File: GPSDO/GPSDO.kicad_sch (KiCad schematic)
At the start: 119 parts, among them IC4 74HC14, IC5 74HC14, IC7 74HC14, IC8 74HC14, J11 JP1, J2 SolderJumper_3_Open, J3 SolderJumper_2_Open, K1 Conn_01x04, K10 Conn_Coaxial, K3 Conn_01x02, K4 Conn_Coaxial, K5 Jumper_3_Open, K6 Conn_Coaxial, K7 Conn_01x02, K8 Conn_Coaxial, K9 Conn_Coaxial, U1 LM7805_TO220, U2 DAC8571IDGK, U3 Pico, U4 AD8620, U5 74LVC2G86, U6 LM4040DBZ-4.1, U8 U1, U9 CAT24C128

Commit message: Layout almost done (GND plane & edge cuts missing), replaced counters with PIC 12F675 MCU for more flexible down conversion and less ICs on the PCB
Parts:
- removed C36, C37: 100n, Capacitor_SMD:C_1210_3225Metric_Pad1.33x2.70mm_HandSolder, symbol Device:C
- removed IC3, IC6: ~, Package_SO:SOIC-16_3.9x9.9mm_P1.27mm, symbol GPSDO-Components:CD74HC390_1
- removed IC4, IC5, IC8: 74HC14, Package_SO:SOIC-14_3.9x8.7mm_P1.27mm, symbol 74xx:74HC14
- removed J11: JP1, Connector_PinHeader_2.54mm:PinHeader_2x03_P2.54mm_Vertical, symbol Connector_Generic:Conn_02x03_Counter_Clockwise
- removed J2: SolderJumper_3_Open, Jumper:SolderJumper-3_P1.3mm_Open_RoundedPad1.0x1.5mm_NumberLabels, symbol Jumper:SolderJumper_3_Open
- removed J3: SolderJumper_2_Open, Jumper:SolderJumper-2_P1.3mm_Open_RoundedPad1.0x1.5mm, symbol Jumper:SolderJumper_2_Open
- removed L11: 10µ, Inductor_SMD:L_0805_2012Metric_Pad1.15x1.40mm_HandSolder, symbol Device:L
- added JP2: Conn_02x03_Odd_Even, Connector_PinHeader_2.54mm:PinHeader_2x03_P2.54mm_Vertical, symbol Connector_Generic:Conn_02x03_Odd_Even
- added U10, U7: 74HC14, Package_SO:SOIC-14_3.9x8.7mm_P1.27mm, symbol 74xx:74HC14
- added U11: PIC12F675-xP, Package_DIP:DIP-8_W7.62mm, symbol MCU_Microchip_PIC12:PIC12F675-xP
- C11, C3: footprint Capacitor_THT:C_Rect_L7.2mm_W3.5mm_P5.00mm_FKS2_FKP2_MKS2_MKP2 -> Capacitor_THT:C_Rect_L7.2mm_W5.5mm_P5.00mm_FKS2_FKP2_MKS2_MKP2
- C17, C2, C21, C7: footprint Capacitor_THT:CP_Radial_D6.3mm_P2.50mm -> Capacitor_SMD:CP_Elec_4x5.3
- C18, C5: footprint Capacitor_THT:CP_Radial_D10.0mm_P5.00mm -> Capacitor_SMD:CP_Elec_6.3x9.9
- D1: footprint Diode_SMD:D_SMA-SMB_Universal_Handsoldering -> Diode_SMD:D_SOD-123F
- D2: footprint Diode_THT:D_DO-15_P10.16mm_Horizontal -> Diode_SMD:D_SMB
- K7: footprint Connector_BarrelJack:BarrelJack_CUI_PJ-102AH_Horizontal -> Connector_AMASS:AMASS_XT30PW-M_1x02_P2.50mm_Horizontal
- R1, R10, R11, R12, R13, R14, R15, R16, R17, R18, R19, R2, R20, R21, R22, R23, R24, R25, R26, R27, R28, R29, R3, R30, R31, R32, R33, R34, R35, R36, R37, R38, R39, R4, R40, R41, R42, R43, R5, R6, R7, R8, R9: footprint Resistor_SMD:R_1210_3225Metric_Pad1.30x2.65mm_HandSolder -> Resistor_SMD:R_0805_2012Metric_Pad1.20x1.40mm_HandSolder
- RV1: footprint Potentiometer_THT:Potentiometer_Bourns_3266Y_Vertical -> Potentiometer_SMD:Potentiometer_Bourns_3314S_Horizontal
- RV2: footprint Potentiometer_THT:Potentiometer_Bourns_3266Y_Vertical -> Potentiometer_SMD:Potentiometer_Bourns_3314J_Vertical
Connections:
- net GND: now also JP2.5 (Pin_5), JP2.6 (Pin_6), U10.7 (GND), U11.8 (VSS), U7.7 (GND)
- net VCC: no longer R3.1
- net at L7.2: now also C26.2, U11.1 (VDD)
- net at R29.1: now also U11.7 (GP0)
- net at U5.7: now also U7.1, U7.11, U7.13, U7.3
- net at R34.2: now also U7.10
- net at U8.5 (CLK): now also U10.11, U10.3, U10.5, U10.9
- net at R18.2: now also U10.4
- net at U5.3: now also U10.1, U10.13, U7.5, U7.9
- net at R21.2: now also U7.6
- net at R30.2: now also U7.8
- net at R18.1, R40.1, R42.1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: now also K10.1 (In)
- net at R43.2: now also U10.10
- net at C35.1, L2.1, R38.2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: now also R3.1
- net at U8.4 (S1): now also JP2.3 (Pin_3)
- net at U8.6 (S0): now also JP2.4 (Pin_4)
- net at C25.2, L6.2: now also U10.14 (VCC)
- net at IC7.11, IC7.13, IC7.2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: now also U11.2 (GP5)
- net at R42.2: now also U10.8
- net at C24.2, L4.2: now also U7.14 (VCC)
- net at R40.2: now also U10.6
- net at R31.2: now also U10.2
- net at R32.2: now also U10.12
- net at R39.2: now also JP2.2 (Pin_2)
- net at R33.2: now also U7.4
- net at R38.1: now also JP2.1 (Pin_1)
- net at R41.2: now also U7.12
- net at R19.2: now also U7.2
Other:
- note added: "10MHz_in"
- note added: "1kHz/10kHz/100kHz from GPS module"
- note added: "CLK_out"
- note added: "D2 Entstördiode https://www.mouser.de/ProductDetail/Micro-Commercial-Components-MCC/SMBJP6KE6.8CA-TP?qs=O1HRStiETCjFEvwWmakxhQ%3D%3D"
- note removed: "100kHz"
- note removed: "10kHz"
- note removed: "1MHz"
- note removed: "1kHz"
- note removed: "Bypass IC3"
- note removed: "D2 Entstördiode https://www.mouser.de/ProductDetail/Nexperia/PESD5V5H1BSFYL?qs=T3oQrply3y9CfA%2FMHqAcog%3D%3D"
- note removed: "close: f_comp=100kHz"
- moved on the sheet: C24, C25, K10, L4, L6

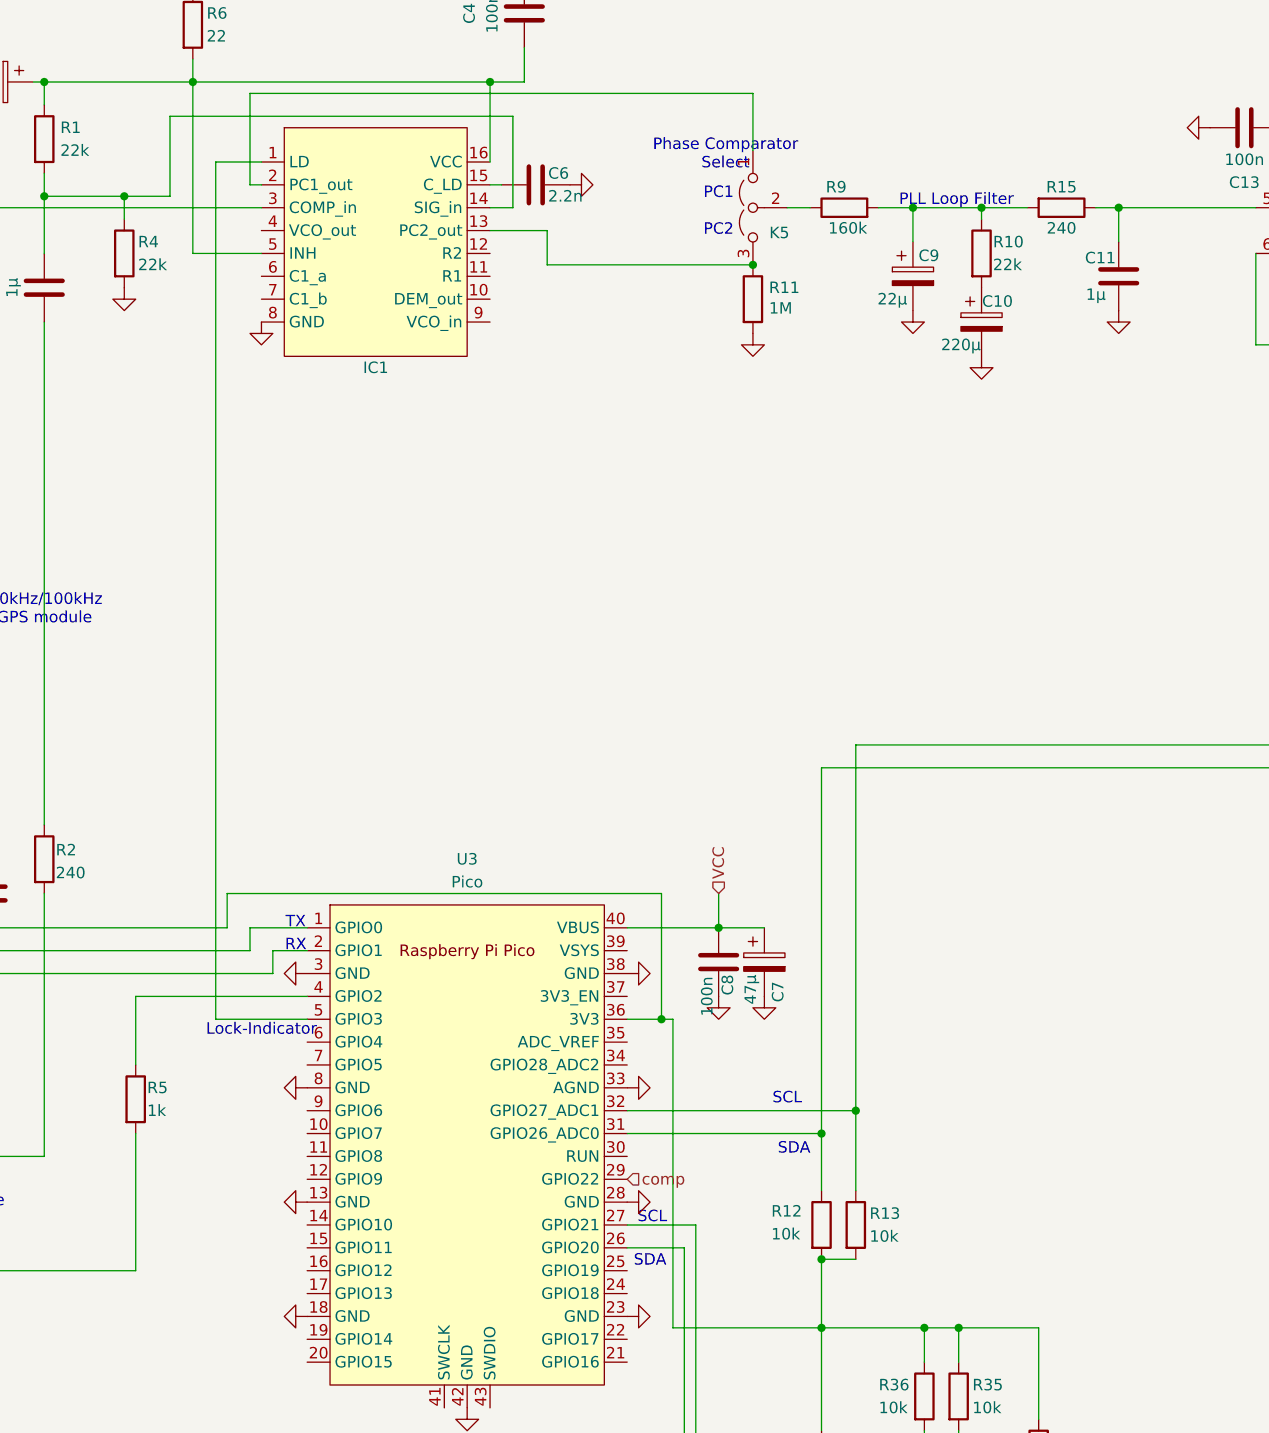
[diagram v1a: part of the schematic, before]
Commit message: VCC net width fix, added voltage dividers for Pico inputs
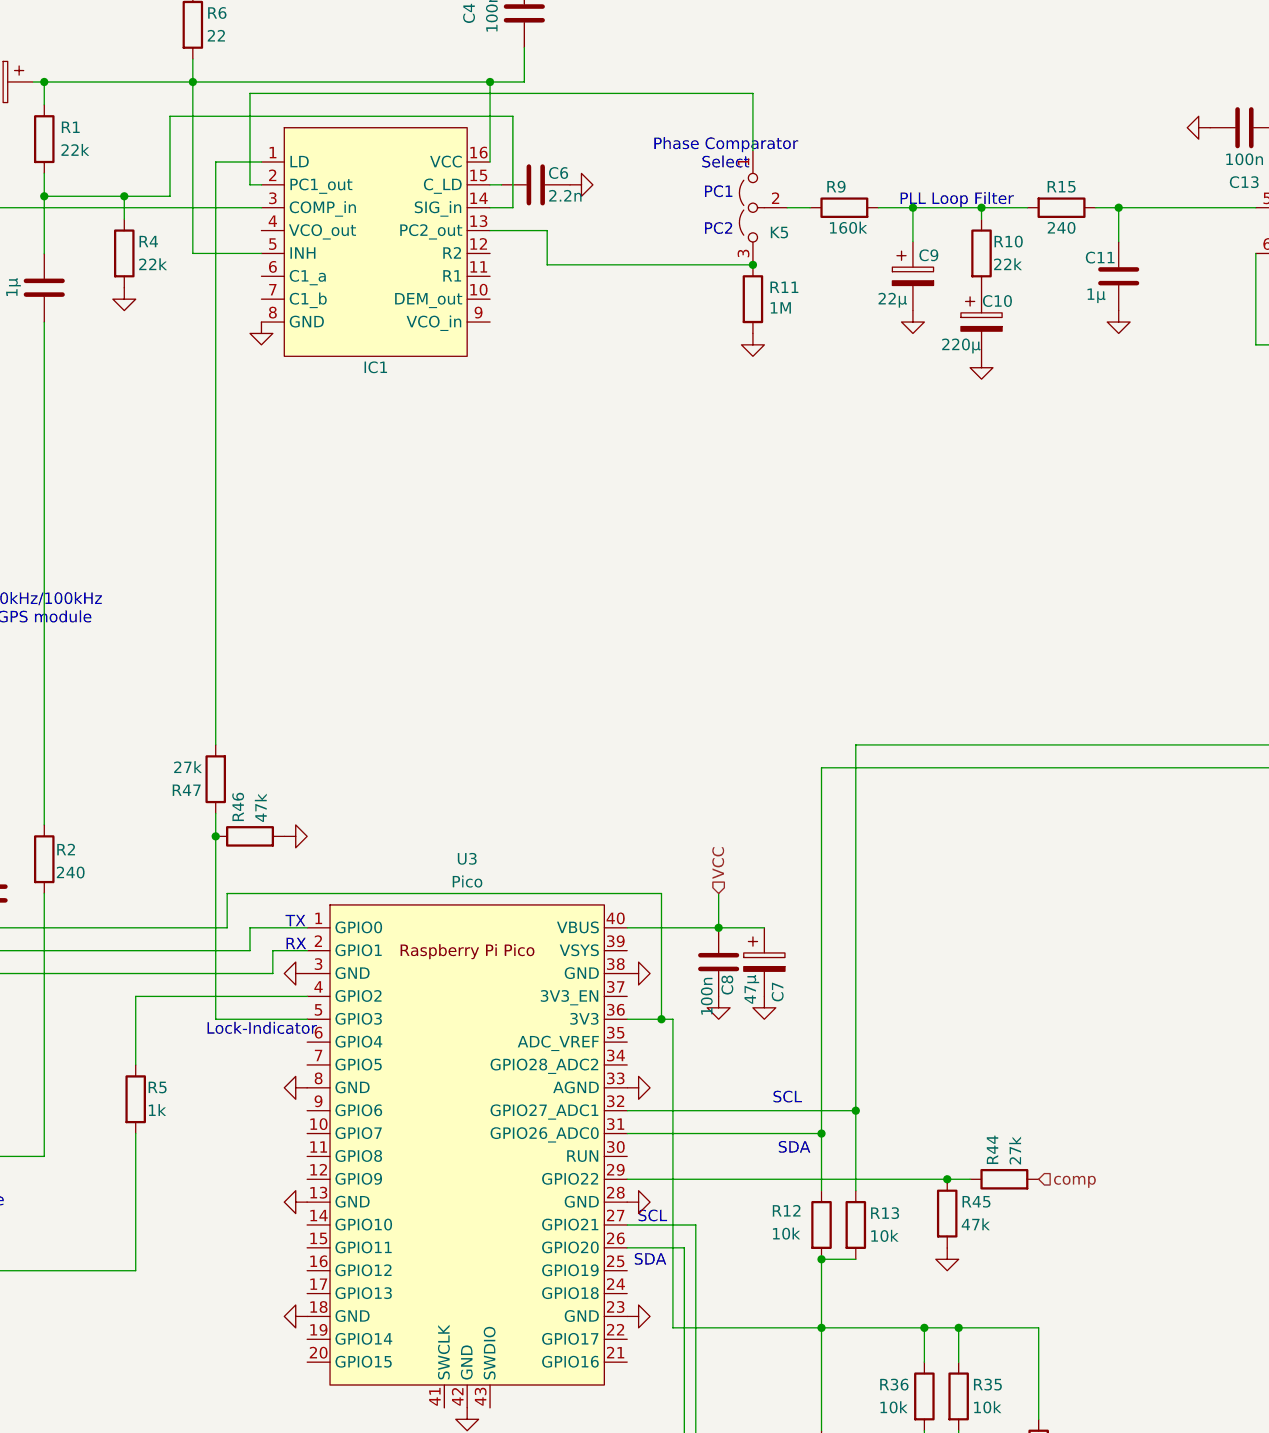
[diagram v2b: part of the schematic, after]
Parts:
- added R44, R47: 27k, Resistor_SMD:R_0805_2012Metric_Pad1.20x1.40mm_HandSolder, symbol Device:R
- added R45, R46: 47k, Resistor_SMD:R_0805_2012Metric_Pad1.20x1.40mm_HandSolder, symbol Device:R
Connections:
- net GND: now also R45.2, R46.2
- net comp: now also R44.2; no longer U3.29 (GPIO22)
- net at U3.5 (GPIO3): now also R46.1, R47.1; no longer IC1.1 (LD)
- new net: IC1.1 (LD), R47.2
- new net: R44.1, R45.1, U3.29 (GPIO22)

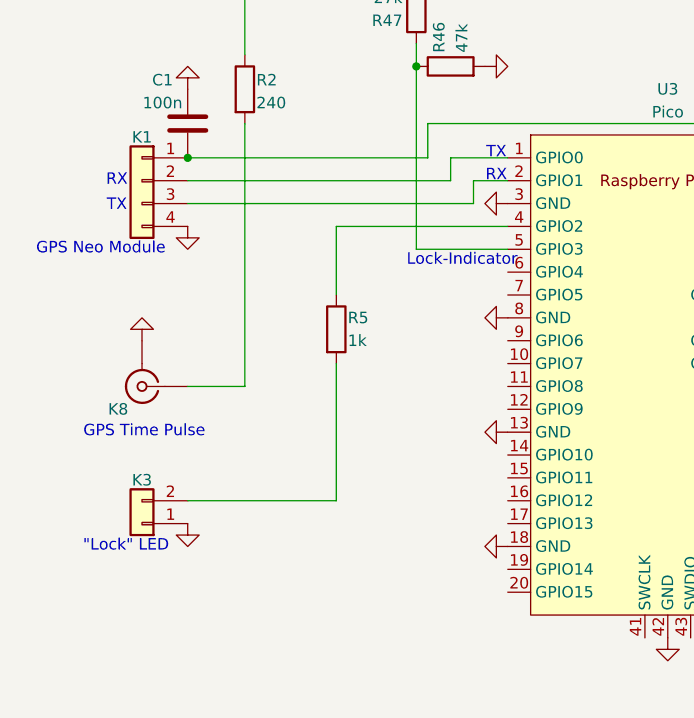
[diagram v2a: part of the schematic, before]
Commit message: Added GPSDO prototype schematic with DIP ICs
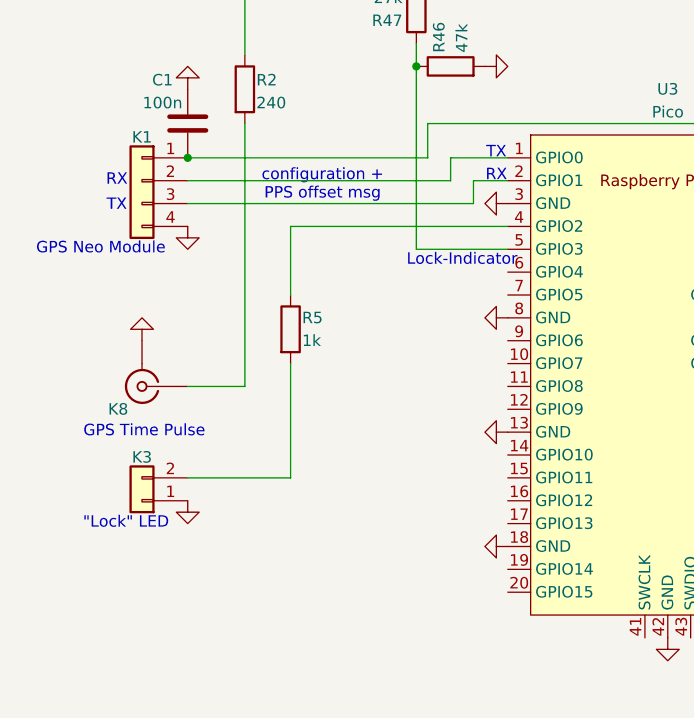
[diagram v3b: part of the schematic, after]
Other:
- note added: "configuration + PPS offset msg"
- moved on the sheet: K3, R5
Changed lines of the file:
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@@
 	(wire
 		(pts
-			(xy 46.99 213.36) (xy 30.48 213.36)
+			(xy 41.91 210.82) (xy 30.48 210.82)
 		)
 		(stroke
@@
 	(wire
 		(pts
-			(xy 66.04 182.88) (xy 46.99 182.88)
+			(xy 66.04 182.88) (xy 41.91 182.88)
 		)
 		(stroke
@@
 	(wire
 		(pts
-			(xy 46.99 198.12) (xy 46.99 213.36)
+			(xy 41.91 198.12) (xy 41.91 210.82)
 		)
 		(stroke
@@
 	(wire
 		(pts
-			(xy 46.99 182.88) (xy 46.99 190.5)
+			(xy 41.91 182.88) (xy 41.91 190.5)
 		)
 		(stroke
@@
 		)
 	)
+	(text "configuration +\nPPS offset msg"
+		(exclude_from_sim no)
+		(at 45.466 178.308 0)
+		(effects
+			(font
+				(size 1.27 1.27)
+			)
+		)
+	)
 	(text "25mA\nSMD klein"
 		(exclude_from_sim no)
@@
 	(text "\"Lock\" LED"
 		(exclude_from_sim no)
-		(at 23.622 218.44 0)
+		(at 23.622 215.9 0)
 		(effects
 			(font
@@
 	(symbol
 		(lib_id "power:GND")
-		(at 30.48 215.9 0)
+		(at 30.48 213.36 0)
 		(unit 1)
 		(exclude_from_sim no)
@@
 		(fields_autoplaced yes)
 		(property "Reference" "#PWR07"
-			(at 30.48 222.25 0)
+			(at 30.48 219.71 0)
 			(effects
 				(font
@@
 		)
 		(property "Value" "GND"
-			(at 30.48 220.98 0)
+			(at 30.48 218.44 0)
 			(effects
 				(font
@@
 		)
 		(property "Footprint" ""
-			(at 30.48 215.9 0)
+			(at 30.48 213.36 0)
 			(effects
 				(font
@@
 		)
 		(property "Datasheet" ""
-			(at 30.48 215.9 0)
+			(at 30.48 213.36 0)
 			(effects
 				(font
@@
 		)
 		(property "Description" "Power symbol creates a global label with name \"GND\" , ground"
-			(at 30.48 215.9 0)
+			(at 30.48 213.36 0)
 			(effects
 				(font
@@
 	(symbol
 		(lib_id "Device:R")
-		(at 46.99 194.31 0)
+		(at 41.91 194.31 0)
 		(unit 1)
 		(exclude_from_sim no)
@@
 		(dnp no)
 		(property "Reference" "R5"
-			(at 48.26 193.04 0)
+			(at 43.18 193.04 0)
 			(effects
 				(font
@@
 		)
 		(property "Value" "1k"
-			(at 48.26 195.58 0)
+			(at 43.18 195.58 0)
 			(effects
 				(font
@@
 		)
 		(property "Footprint" "Resistor_SMD:R_0805_2012Metric_Pad1.20x1.40mm_HandSolder"
-			(at 45.212 194.31 90)
+			(at 40.132 194.31 90)
 			(effects
 				(font
@@
 		)
 		(property "Datasheet" "~"
-			(at 46.99 194.31 0)
+			(at 41.91 194.31 0)
 			(effects
 				(font
@@
 		)
 		(property "Description" "Resistor"
-			(at 46.99 194.31 0)
+			(at 41.91 194.31 0)
 			(effects
 				(font
@@
 	(symbol
 		(lib_id "Connector_Generic:Conn_01x02")
-		(at 25.4 215.9 180)
+		(at 25.4 213.36 180)
 		(unit 1)
 		(exclude_from_sim no)
@@
 		(dnp no)
 		(property "Reference" "K3"
-			(at 25.4 211.074 0)
+			(at 25.4 208.534 0)
 			(effects
 				(font
@@
 		)
 		(property "Value" "Conn_01x02"
-			(at 25.4 209.55 0)
+			(at 25.4 207.01 0)
 			(effects
 				(font
@@
 		)
 		(property "Footprint" "Connector_PinHeader_2.54mm:PinHeader_1x02_P2.54mm_Vertical"
-			(at 25.4 215.9 0)
+			(at 25.4 213.36 0)
 			(effects
 				(font
@@
 		)
 		(property "Datasheet" "~"
-			(at 25.4 215.9 0)
+			(at 25.4 213.36 0)
 			(effects
 				(font
@@
 		)
 		(property "Description" "Generic connector, single row, 01x02, script generated (kicad-library-utils/schlib/autogen/connector/)"
-			(at 25.4 215.9 0)
+			(at 25.4 213.36 0)
 			(effects
 				(font
